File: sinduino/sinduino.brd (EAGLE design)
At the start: 100 x 80 mm, 23 parts, among them IC1 IC_UC_ATMEGA32U4-TQFP44, Q1 16000, X1 MINI-USB-32005-301

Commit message: proceed connecting
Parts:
- added LED4: yellow, led:LED3MM
- added R6: 680, rcl:R1206
- moved C4 7.73 mm to (55.9, 20.3)
- moved IC1 6.35 mm to (43.8, 17.1)
- moved C5 5.08 mm to (52.7, 9.53)
- moved C6 2.54 mm to (32.4, 12.7)
- moved C7 1.42 mm to (33.7, 7.62)
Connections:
- new net D0: IC1.P20, JP2.13
- new net D1: IC1.P21, JP2.14
- new net D12: IC1.P26, JP2.16
- new net D2: IC1.P19, JP2.12
- new net D4: IC1.P25, JP2.15
- new net D6: IC1.P27, JP2.17
- new net N$11: LED4.K, R6.2
- new net N$2: IC1.P22, R6.1
- net VCC: now also LED4.A

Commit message: almost connected everything
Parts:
- added IC2: TS2940CT5TV, n39:TO220V
- added R5: 3k9, rcl:R1206
- added U$3: RIACON_101_2, n39:RIACON_101_2
- C1: value 100u -> 470n; device rcl:E2,5-6 -> rcl:C025-025X050
- C2: value 100u -> 33u
- moved C1 27.3 mm to (13.3, 27.3)
- moved C2 26.7 mm to (12.1, 20.3)
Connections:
- new net A0: IC1.P36, JP3.6
- new net A1: IC1.P37, JP3.7
- new net A2: IC1.P38, JP3.8
- new net A3: IC1.P39, JP3.9
- new net A4: IC1.P40, JP3.10
- new net A5: IC1.P41, JP3.11
- new net AREF: C7.1, IC1.P42, JP3.12
- new net D13: IC1.P32, JP3.5
- new net D5: IC1.P31, JP3.4
- new net D7: IC1.P1, JP3.13
- new net HWB: IC1.P33, R5.2
- new net N$12: IC1.P29, JP3.2
- new net N$13: IC1.P28, JP3.1
- new net N$15: C1.1, IC2.1, U$3.2
- new net N$16: C2.+, IC2.3, JP1.3
- net GND: now also C1.2, C2.-, IC2.2, R5.1, U$3.1
- net N$1: now also IC1.P30, JP3.3; no longer C7.1, IC1.P42
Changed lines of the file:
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@@
 <elements>
 <element name="IC1" library="dp_devices" package="TQFP-44" value="IC_UC_ATMEGA32U4-TQFP44" x="43.815" y="17.145" rot="MR90"/>
-<element name="C1" library="rcl" package="E2,5-6" value="100u" x="13.97" y="54.61" rot="R270"/>
-<element name="C2" library="rcl" package="E2,5-6" value="100u" x="13.97" y="46.99" rot="R90"/>
+<element name="C1" library="rcl" package="C025-025X050" value="470n" x="13.335" y="27.305" rot="R270"/>
+<element name="C2" library="rcl" package="E2,5-6" value="33u" x="12.065" y="20.32" rot="R90"/>
 <element name="C3" library="rcl" package="C1206" value="100n" x="54.61" y="39.37" rot="MR180"/>
 <element name="C4" library="rcl" package="C1206" value="100n" x="55.88" y="20.32" rot="MR0"/>
@@
 <element name="R6" library="rcl" package="R1206" value="680" x="52.705" y="23.495" rot="MR0"/>
 <element name="LED4" library="led" package="LED3MM" value="yellow" x="53.34" y="27.94"/>
+<element name="R5" library="rcl" package="R1206" value="3k9" x="55.88" y="10.795" rot="MR90"/>
+<element name="IC2" library="n39" package="TO220V" value="TS2940CT5TV" x="19.685" y="26.035" rot="R270">
+<attribute name="REICHELT" value="LM 2940 CT5" x="19.685" y="26.035" size="1.778" layer="27" rot="R270" display="off"/>
+</element>
+<element name="U$3" library="n39" package="RIACON_101_2" value="RIACON_101_2" x="5.715" y="27.305" rot="R180">
+<attribute name="REICHELT" value="AKL 101-02" x="5.715" y="27.305" size="1.778" layer="27" rot="R180" display="off"/>
+</element>
 </elements>
 <signals>
@@
 <contactref element="JP3" pad="15"/>
 <contactref element="JP3" pad="14"/>
+<contactref element="R5" pad="1"/>
+<contactref element="IC2" pad="2"/>
+<contactref element="C1" pad="2"/>
+<contactref element="C2" pad="-"/>
+<contactref element="U$3" pad="1"/>
 <wire x1="61.09" y1="48.26" x2="66.17" y2="48.26" width="0" layer="19" extent="16-16"/>
 <wire x1="56.01" y1="39.37" x2="61.09" y2="48.26" width="0" layer="19" extent="16-16"/>
@@
 <wire x1="47.015" y1="11.445" x2="40.615" y2="11.445" width="0" layer="19" extent="16-16"/>
 <wire x1="52.705" y1="8.125" x2="47.015" y2="11.445" width="0" layer="19" extent="16-16"/>
+<wire x1="55.88" y1="9.373" x2="52.705" y2="8.125" width="0" layer="19" extent="16-16"/>
 <wire x1="21.72" y1="5.715" x2="32.255" y2="7.62" width="0" layer="19" extent="16-16"/>
 <wire x1="17.3" y1="3" x2="21.72" y2="5.715" width="0" layer="19" extent="16-16"/>
@@
 <wire x1="9.68" y1="3" x2="12.22" y2="3" width="0" layer="19" extent="1-1"/>
 <wire x1="9" y1="20.1" x2="9.68" y2="3" width="0" layer="19" extent="16-16"/>
-<wire x1="26.54" y1="30.48" x2="42.215" y2="22.845" width="0" layer="19" extent="16-16"/>
+<wire x1="12.065" y1="21.59" x2="9" y2="20.1" width="0" layer="19" extent="16-16"/>
+<wire x1="13.335" y1="26.035" x2="12.065" y2="21.59" width="0" layer="19" extent="1-1"/>
+<wire x1="17.145" y1="26.035" x2="13.335" y2="26.035" width="0" layer="19" extent="1-1"/>
+<wire x1="8.255" y1="27.305" x2="13.335" y2="26.035" width="0" layer="19" extent="1-1"/>
+<wire x1="26.54" y1="30.48" x2="17.145" y2="26.035" width="0" layer="19" extent="16-16"/>
 <wire x1="34.58" y1="44.375" x2="26.54" y2="30.48" width="0" layer="19" extent="16-16"/>
 <wire x1="34.58" y1="50.875" x2="34.58" y2="44.375" width="0" layer="19" extent="1-1"/>
-</signal>
-<signal name="N$1">
-<contactref element="IC1" pad="P42"/>
-<contactref element="C7" pad="1"/>
-<wire x1="35.055" y1="7.62" x2="41.415" y2="11.445" width="0" layer="19" extent="16-16"/>
 </signal>
 <signal name="N$3">
@@
 <wire x1="51.283" y1="23.495" x2="54.61" y2="27.94" width="0" layer="19" extent="16-16"/>
 </signal>
+<signal name="D7">
+<contactref element="JP3" pad="13"/>
+<contactref element="IC1" pad="P1"/>
+<wire x1="19.84" y1="3" x2="38.115" y2="13.145" width="0" layer="19" extent="16-16"/>
+</signal>
+<signal name="AREF">
+<contactref element="JP3" pad="12"/>
+<contactref element="IC1" pad="P42"/>
+<contactref element="C7" pad="1"/>
+<wire x1="35.055" y1="7.62" x2="41.415" y2="11.445" width="0" layer="19" extent="16-16"/>
+<wire x1="22.38" y1="3" x2="35.055" y2="7.62" width="0" layer="19" extent="16-16"/>
+</signal>
+<signal name="A5">
+<contactref element="IC1" pad="P41"/>
+<contactref element="JP3" pad="11"/>
+<wire x1="24.92" y1="3" x2="42.215" y2="11.445" width="0" layer="19" extent="16-16"/>
+</signal>
+<signal name="A4">
+<contactref element="IC1" pad="P40"/>
+<contactref element="JP3" pad="10"/>
+<wire x1="27.46" y1="3" x2="43.015" y2="11.445" width="0" layer="19" extent="16-16"/>
+</signal>
+<signal name="A3">
+<contactref element="IC1" pad="P39"/>
+<contactref element="JP3" pad="9"/>
+<wire x1="30" y1="3" x2="43.815" y2="11.445" width="0" layer="19" extent="16-16"/>
+</signal>
+<signal name="A2">
+<contactref element="IC1" pad="P38"/>
+<contactref element="JP3" pad="8"/>
+<wire x1="32.54" y1="3" x2="44.615" y2="11.445" width="0" layer="19" extent="16-16"/>
+</signal>
+<signal name="A1">
+<contactref element="IC1" pad="P37"/>
+<contactref element="JP3" pad="7"/>
+<wire x1="35.08" y1="3" x2="45.415" y2="11.445" width="0" layer="19" extent="16-16"/>
+</signal>
+<signal name="A0">
+<contactref element="IC1" pad="P36"/>
+<contactref element="JP3" pad="6"/>
+<wire x1="37.62" y1="3" x2="46.215" y2="11.445" width="0" layer="19" extent="16-16"/>
+</signal>
+<signal name="D13">
+<contactref element="IC1" pad="P32"/>
+<contactref element="JP3" pad="5"/>
+<wire x1="40.16" y1="3" x2="49.515" y2="13.945" width="0" layer="19" extent="16-16"/>
+</signal>
+<signal name="D5">
+<contactref element="IC1" pad="P31"/>
+<contactref element="JP3" pad="4"/>
+<wire x1="42.7" y1="3" x2="49.515" y2="14.745" width="0" layer="19" extent="16-16"/>
+</signal>
+<signal name="N$1">
+<contactref element="JP3" pad="3"/>
+<contactref element="IC1" pad="P30"/>
+<wire x1="45.24" y1="3" x2="49.515" y2="15.545" width="0" layer="19" extent="16-16"/>
+</signal>
+<signal name="N$12">
+<contactref element="IC1" pad="P29"/>
+<contactref element="JP3" pad="2"/>
+<wire x1="47.78" y1="3" x2="49.515" y2="16.345" width="0" layer="19" extent="16-16"/>
+</signal>
+<signal name="N$13">
+<contactref element="JP3" pad="1"/>
+<contactref element="IC1" pad="P28"/>
+<wire x1="50.32" y1="3" x2="49.515" y2="17.145" width="0" layer="19" extent="16-16"/>
+</signal>
+<signal name="HWB">
+<contactref element="IC1" pad="P33"/>
+<contactref element="R5" pad="2"/>
+<wire x1="49.515" y1="13.145" x2="55.88" y2="12.217" width="0" layer="19" extent="16-16"/>
+</signal>
+<signal name="N$15">
+<contactref element="IC2" pad="1"/>
+<contactref element="C1" pad="1"/>
+<contactref element="U$3" pad="2"/>
+<wire x1="13.335" y1="28.575" x2="17.145" y2="28.575" width="0" layer="19" extent="1-1"/>
+<wire x1="3.175" y1="27.305" x2="13.335" y2="28.575" width="0" layer="19" extent="1-1"/>
+</signal>
+<signal name="N$16">
+<contactref element="IC2" pad="3"/>
+<contactref element="C2" pad="+"/>
+<contactref element="JP1" pad="3"/>
+<wire x1="12.065" y1="19.05" x2="17.145" y2="23.495" width="0" layer="19" extent="1-1"/>
+<wire x1="17.78" y1="10.16" x2="12.065" y2="19.05" width="0" layer="19" extent="1-1"/>
+</signal>
 </signals>

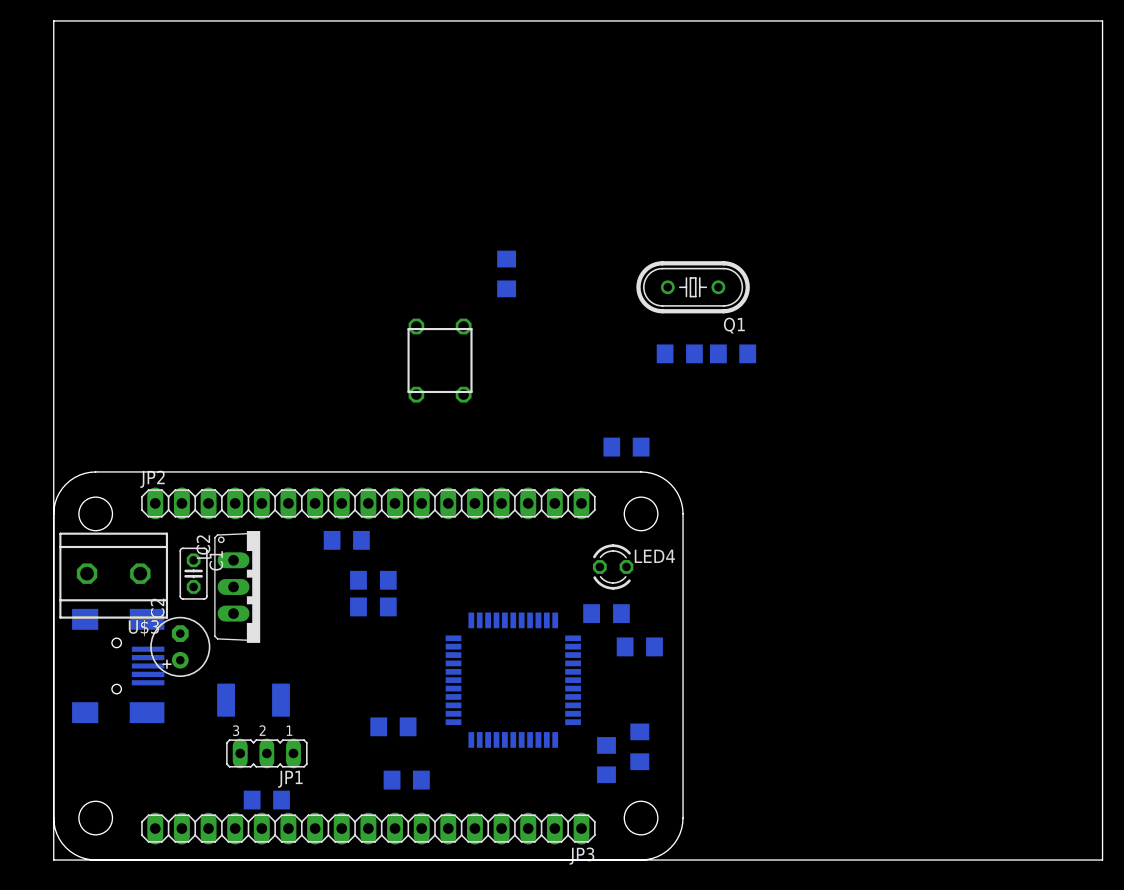
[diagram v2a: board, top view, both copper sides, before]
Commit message: complete schematic and start routing
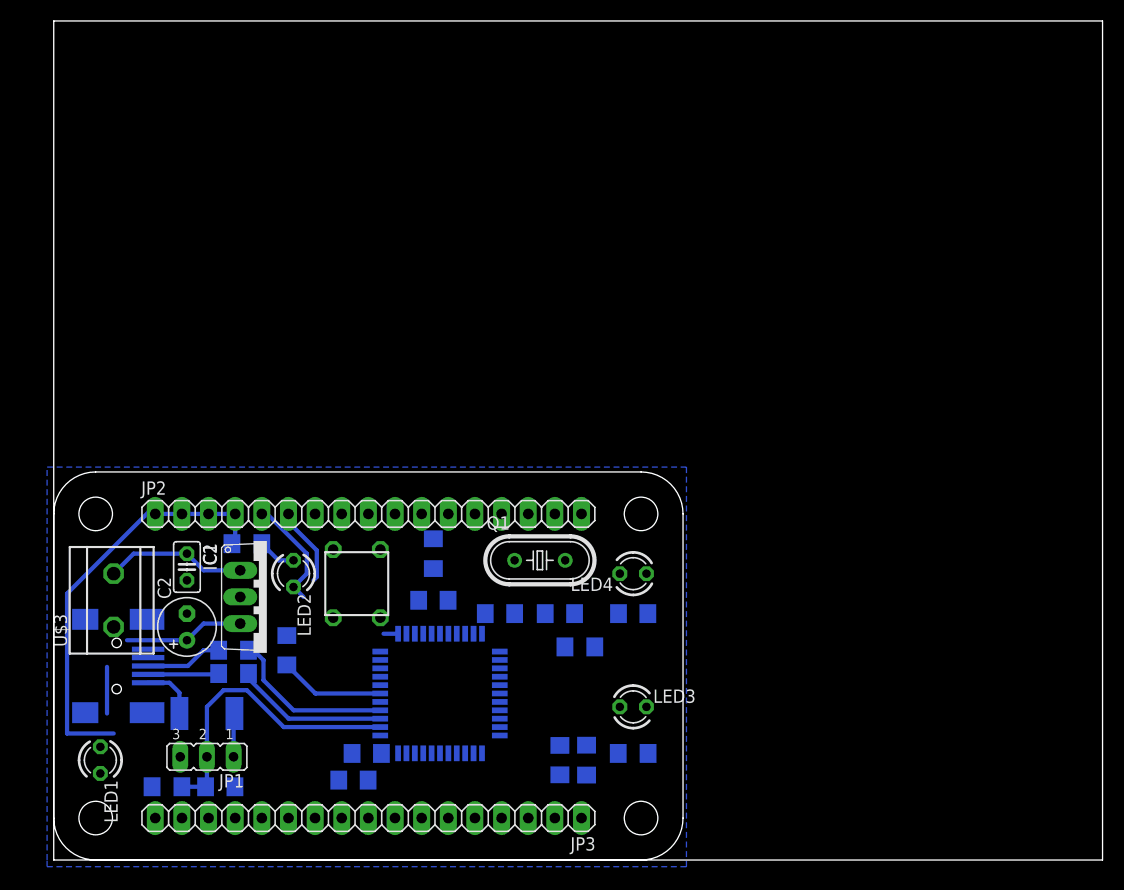
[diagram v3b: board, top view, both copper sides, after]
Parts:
- added LED1: green, led:LED3MM
- added LED2: orange, led:LED3MM
- added LED3: red, led:LED3MM
- added R1, R2, R4: 680, rcl:R1206
- moved C9 33.3 mm to (42.5, 23.5)
- moved Q1 29.9 mm to (46.4, 28.6), turned to 0 degrees
- moved R3 27.6 mm to (36.2, 29.2)
- moved C8 27.3 mm to (48.3, 23.5)
- moved C3 23.5 mm to (36.2, 24.8)
- moved U$1 22.7 mm to (28.9, 26.4)
- moved R8 14.9 mm to (17.1, 20.0)
- moved R7 14.8 mm to (17.1, 17.8)
- moved C10 11.9 mm to (22.2, 20.0), turned to 90 degrees
- moved IC1 7.10 mm to (36.8, 15.9)
- moved JP1 5.72 mm to (14.6, 9.84)
- moved R5 5.24 mm to (50.8, 9.53)
- moved C7 5.08 mm to (28.6, 7.62)
- moved C11 4.62 mm to (15.9, 6.99)
- moved F1 4.62 mm to (14.6, 14.0)
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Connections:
- new net N$14: LED1.A, R1.2
- new net N$17: LED2.A, R2.1
- new net N$18: LED3.A, R4.2
- net D13: now also R4.1
- net D14: now also LED2.K
- net GND: now also LED1.K, LED3.K
- net VCC: now also R1.1, R2.2
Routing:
- net VCC: track 0.00 -> 70.7 mm
- net N$8: track 0.00 -> 16.1 mm
- net N$16: track 0.00 -> 15.9 mm
- net N$9: track 0.00 -> 14.8 mm
- net N$15: track 0.00 -> 13.5 mm
- net D14: track 0.00 -> 11.6 mm
- net N$6: track 0.00 -> 10.0 mm
- net D15: track 0.00 -> 7.58 mm
- net N$7: track 0.00 -> 7.35 mm
- net N$5: track 0.00 -> 6.76 mm
- net N$10: track 0.00 -> 5.36 mm
- net UV: track 0.00 -> 5.24 mm
- net N$17: track 0.00 -> 3.68 mm
- net D11: track 0.00 -> 1.38 mm
- added copper zone on layer 16, net GND

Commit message: proceed routing, move uC, start over …
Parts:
- moved C7 6.03 mm to (22.5, 7.62)
- moved C6 4.46 mm to (25.4, 10.5)
- moved IC1 0.64 mm to (36.8, 16.5)
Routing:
- net D7: track 0.00 -> 17.3 mm
- net AREF: track 0.00 -> 17.3 mm
- net A5: track 0.00 -> 15.2 mm
- net A4: track 0.00 -> 13.5 mm
- net A3: track 0.00 -> 11.9 mm
- net VCC: track 70.7 -> 80.6 mm
- net D11: track 1.38 -> 0.00 mm

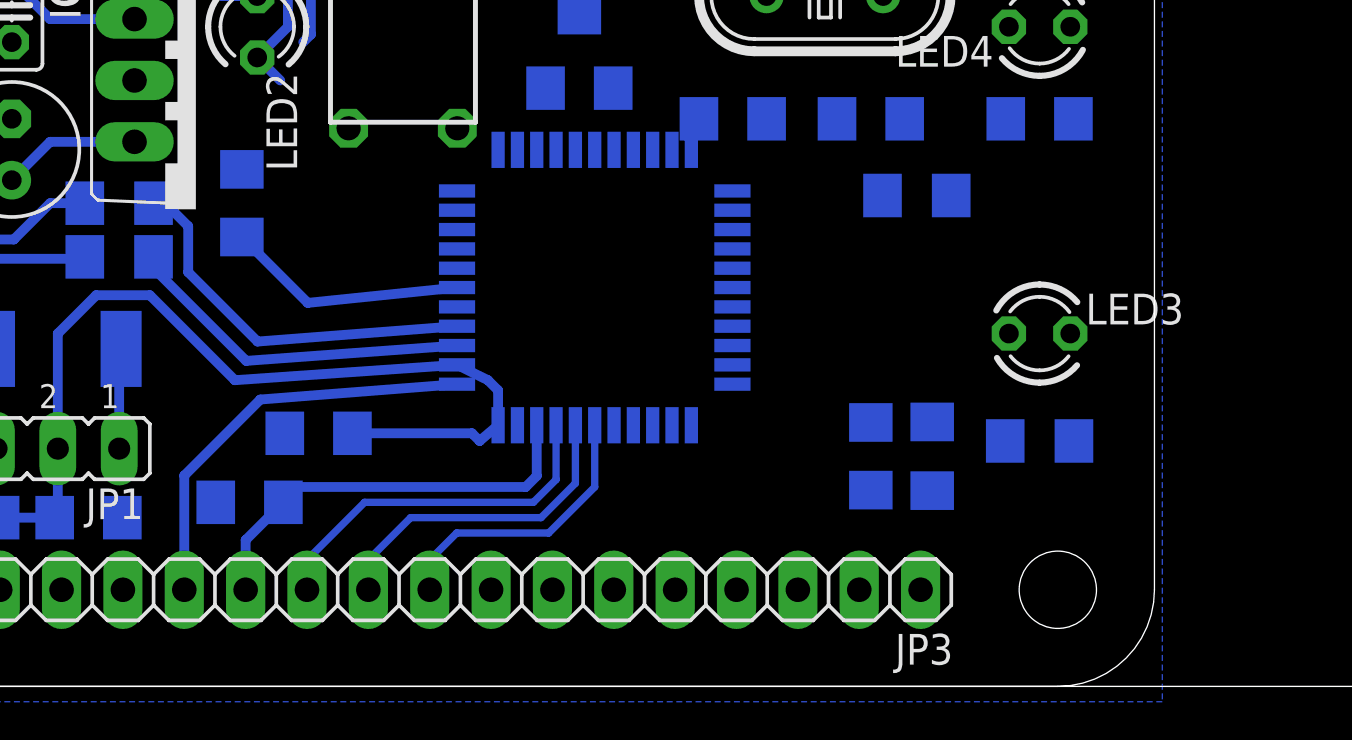
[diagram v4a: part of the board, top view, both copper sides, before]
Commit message: switched one led with its resistor
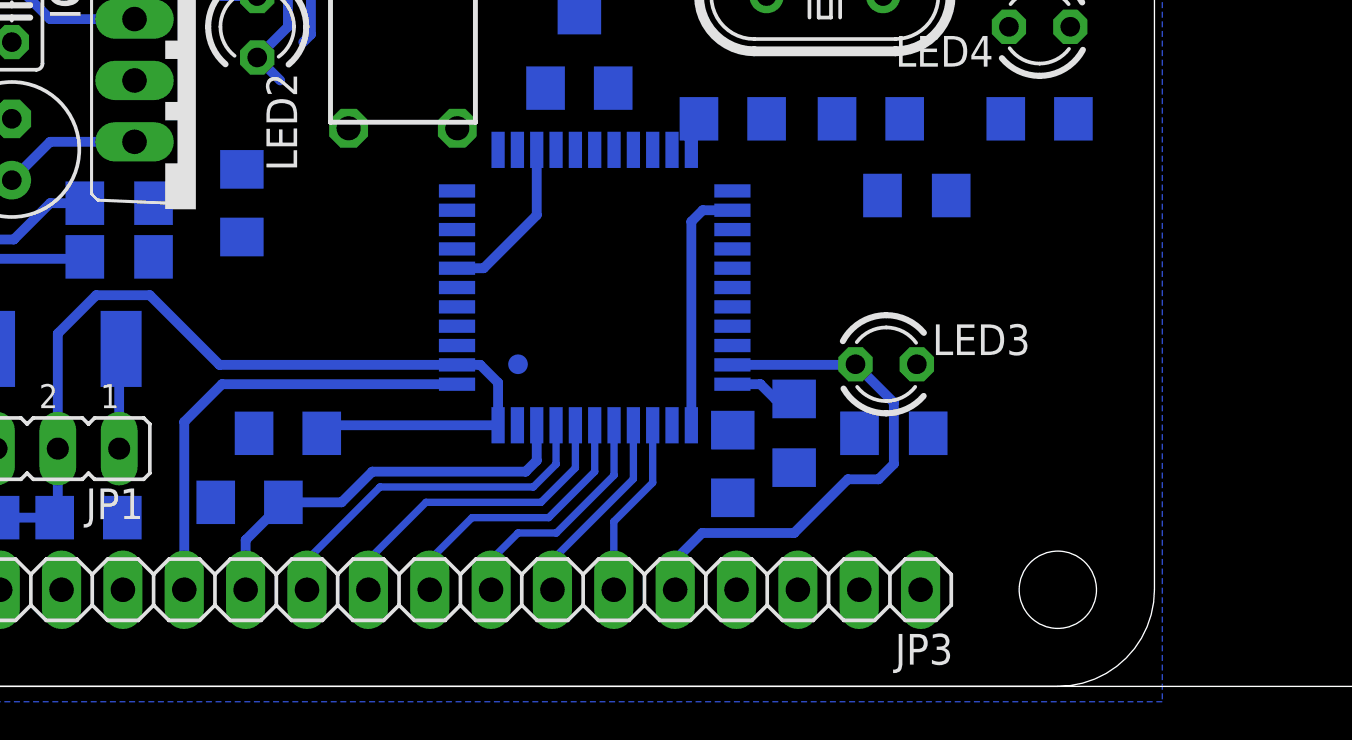
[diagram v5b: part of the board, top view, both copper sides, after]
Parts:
- moved LED3 6.48 mm to (48.9, 13.3)
- moved R4 6.04 mm to (49.2, 10.5)
- moved R5 5.79 mm to (45.1, 10.5)
- moved C5 5.72 mm to (42.5, 9.21)
- moved C6 1.27 mm to (24.1, 10.5)
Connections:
- net D13: now also LED3.A; no longer R4.1
- net GND: now also R4.2; no longer LED3.K
- net N$18: now also LED3.K, R4.1; no longer LED3.A, R4.2
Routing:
- net D13: track 0.00 -> 21.8 mm
- net VCC: track 80.6 -> 98.9 mm
- net N$8: track 16.1 -> 0.00 mm
- net N$9: track 14.8 -> 0.15 mm
- net N$6: track 10.1 -> 0.00 mm
- net A2: track 0.00 -> 9.85 mm
- net A1: track 0.00 -> 8.20 mm
- net A0: track 0.00 -> 7.48 mm
- net HWB: track 0.00 -> 2.81 mm
- net D7: track 17.3 -> 18.9 mm
